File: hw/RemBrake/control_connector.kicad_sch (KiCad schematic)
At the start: 9 parts, among them J4 Conn_01x08_MountingPin, J5 Conn_01x04_MountingPin, J6 Conn_01x03_MountingPin

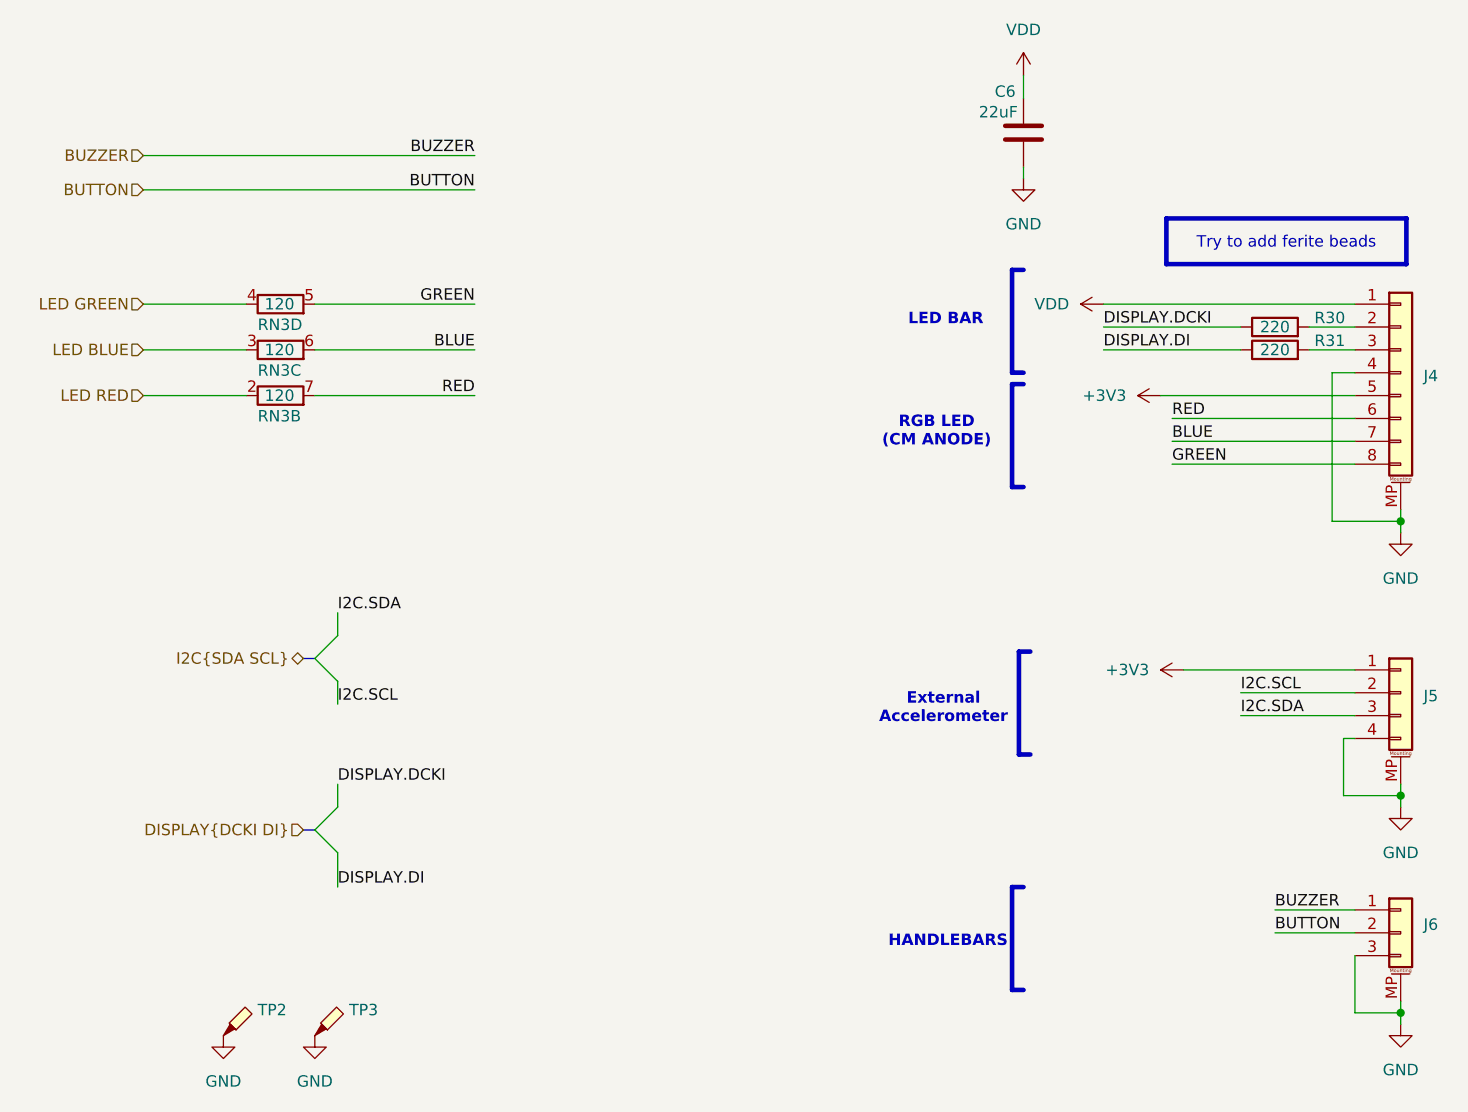
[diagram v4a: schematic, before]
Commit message: added resistor for the ideal diode enable and new annotation
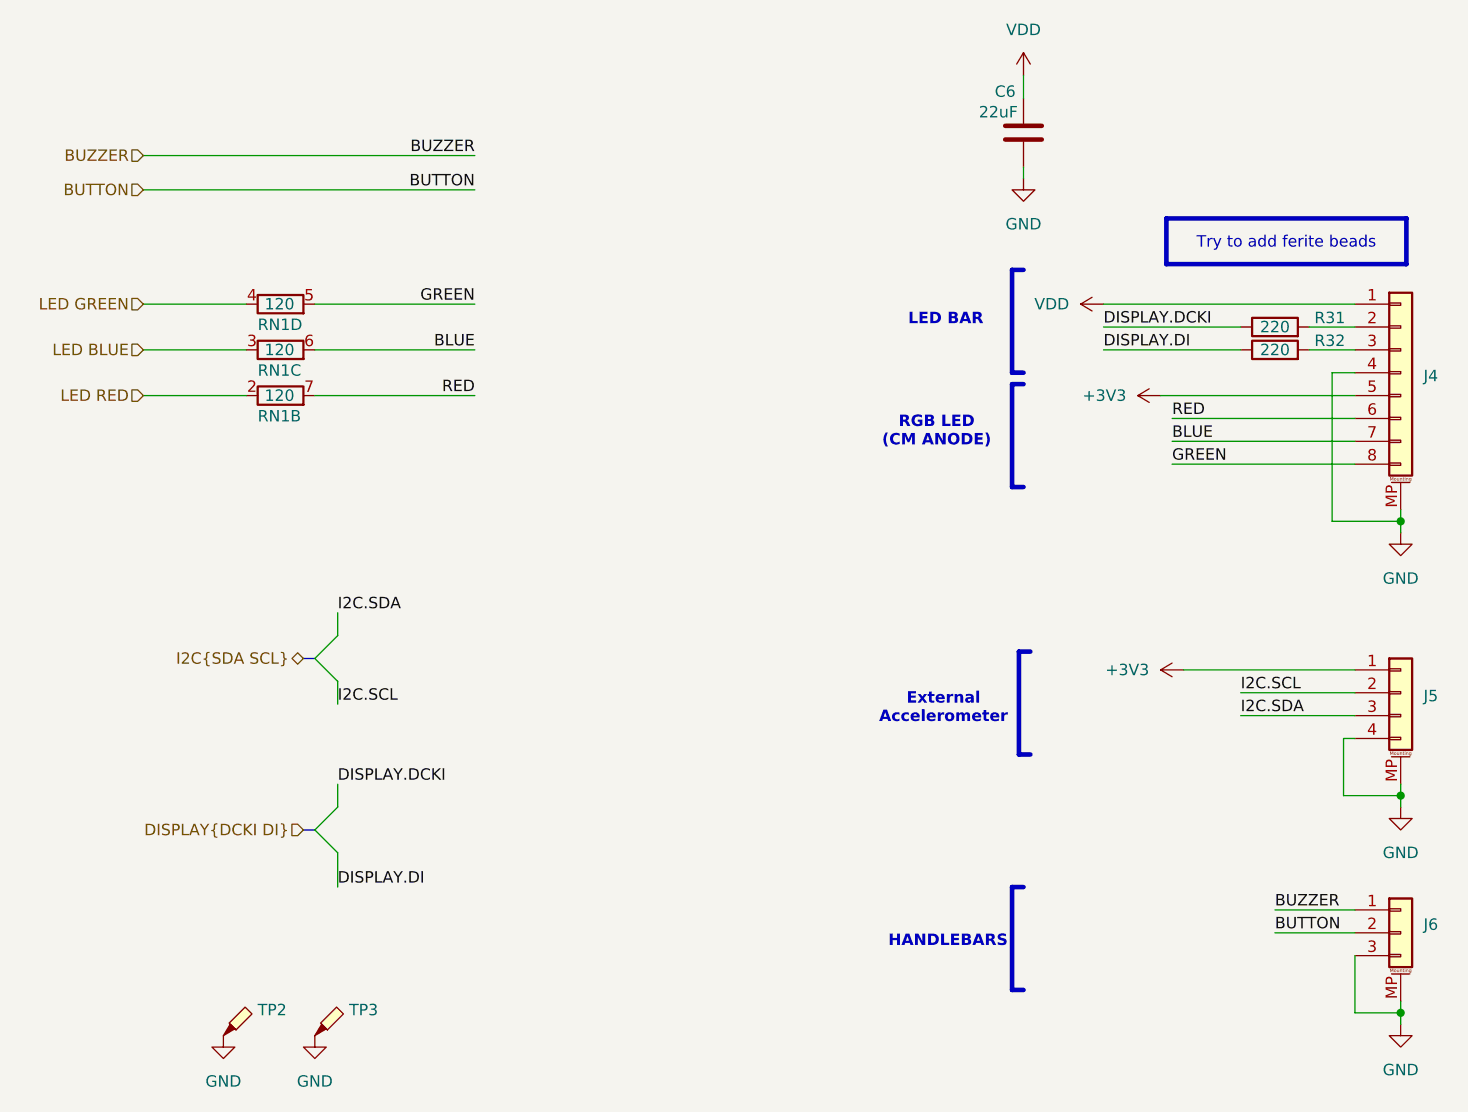
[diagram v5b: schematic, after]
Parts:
- renumbered R30 to R31, R31 to R32, RN3 to RN1
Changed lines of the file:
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@@
 		(dnp no)
 		(fields_autoplaced yes)
-		(property "Reference" "#PWR035"
+		(property "Reference" "#PWR034"
 			(at 96.52 146.05 0)
 			(hide yes)
@@
 			(project "RemBrake"
 				(path "/e6d4ae5b-c9d7-4cbe-b288-c929fdf55a75/c6fda42a-9645-46e5-b66a-57cf8664dccf"
-					(reference "#PWR035")
+					(reference "#PWR034")
 					(unit 1)
 				)
@@
 		(on_board yes)
 		(dnp no)
-		(property "Reference" "RN3"
+		(property "Reference" "RN1"
 			(at 90.17 70.866 90)
 			(effects
@@
 			(project "RemBrake"
 				(path "/e6d4ae5b-c9d7-4cbe-b288-c929fdf55a75/c6fda42a-9645-46e5-b66a-57cf8664dccf"
-					(reference "RN3")
+					(reference "RN1")
 					(unit 2)
 				)
@@
 		(dnp no)
 		(fields_autoplaced yes)
-		(property "Reference" "#PWR041"
+		(property "Reference" "#PWR039"
 			(at 196.85 99.06 0)
 			(hide yes)
@@
 			(project "RemBrake"
 				(path "/e6d4ae5b-c9d7-4cbe-b288-c929fdf55a75/c6fda42a-9645-46e5-b66a-57cf8664dccf"
-					(reference "#PWR041")
+					(reference "#PWR039")
 					(unit 1)
 				)
@@
 		(on_board yes)
 		(dnp no)
-		(property "Reference" "RN3"
+		(property "Reference" "RN1"
 			(at 90.17 60.706 90)
 			(effects
@@
 			(project ""
 				(path "/e6d4ae5b-c9d7-4cbe-b288-c929fdf55a75/c6fda42a-9645-46e5-b66a-57cf8664dccf"
-					(reference "RN3")
+					(reference "RN1")
 					(unit 4)
 				)
@@
 		(on_board yes)
 		(dnp no)
-		(property "Reference" "R30"
+		(property "Reference" "R31"
 			(at 209.296 59.944 90)
 			(effects
@@
 			(project "RemBrake"
 				(path "/e6d4ae5b-c9d7-4cbe-b288-c929fdf55a75/c6fda42a-9645-46e5-b66a-57cf8664dccf"
-					(reference "R30")
+					(reference "R31")
 					(unit 1)
 				)
@@
 		(dnp no)
 		(fields_autoplaced yes)
-		(property "Reference" "#PWR043"
+		(property "Reference" "#PWR041"
 			(at 217.17 120.65 0)
 			(hide yes)
@@
 			(project "RemBrake"
 				(path "/e6d4ae5b-c9d7-4cbe-b288-c929fdf55a75/c6fda42a-9645-46e5-b66a-57cf8664dccf"
-					(reference "#PWR043")
+					(reference "#PWR041")
 					(unit 1)
 				)
@@
 		(dnp no)
 		(fields_autoplaced yes)
-		(property "Reference" "#PWR037"
+		(property "Reference" "#PWR035"
 			(at 175.26 36.83 0)
 			(hide yes)
@@
 			(project "RemBrake"
 				(path "/e6d4ae5b-c9d7-4cbe-b288-c929fdf55a75/c6fda42a-9645-46e5-b66a-57cf8664dccf"
-					(reference "#PWR037")
+					(reference "#PWR035")
 					(unit 1)
 				)
@@
 		(dnp no)
 		(fields_autoplaced yes)
-		(property "Reference" "#PWR042"
+		(property "Reference" "#PWR040"
 			(at 217.17 90.17 0)
 			(hide yes)
@@
 			(project "RemBrake"
 				(path "/e6d4ae5b-c9d7-4cbe-b288-c929fdf55a75/c6fda42a-9645-46e5-b66a-57cf8664dccf"
-					(reference "#PWR042")
+					(reference "#PWR040")
 					(unit 1)
 				)
@@
 		(dnp no)
 		(fields_autoplaced yes)
-		(property "Reference" "#PWR038"
+		(property "Reference" "#PWR036"
 			(at 175.26 50.8 0)
 			(hide yes)
@@
 			(project "RemBrake"
 				(path "/e6d4ae5b-c9d7-4cbe-b288-c929fdf55a75/c6fda42a-9645-46e5-b66a-57cf8664dccf"
-					(reference "#PWR038")
+					(reference "#PWR036")
 					(unit 1)
 				)
@@
 		(dnp no)
 		(fields_autoplaced yes)
-		(property "Reference" "#PWR039"
+		(property "Reference" "#PWR037"
 			(at 187.96 58.42 0)
 			(hide yes)
@@
 			(project ""
 				(path "/e6d4ae5b-c9d7-4cbe-b288-c929fdf55a75/c6fda42a-9645-46e5-b66a-57cf8664dccf"
-					(reference "#PWR039")
+					(reference "#PWR037")
 					(unit 1)
 				)
@@
 		(on_board yes)
 		(dnp no)
-		(property "Reference" "R31"
+		(property "Reference" "R32"
 			(at 209.296 62.484 90)
 			(effects
@@
 			(project "RemBrake"
 				(path "/e6d4ae5b-c9d7-4cbe-b288-c929fdf55a75/c6fda42a-9645-46e5-b66a-57cf8664dccf"
-					(reference "R31")
+					(reference "R32")
 					(unit 1)
 				)
@@
 		(dnp no)
 		(fields_autoplaced yes)
-		(property "Reference" "#PWR034"
+		(property "Reference" "#PWR033"
 			(at 86.36 146.05 0)
 			(hide yes)
@@
 			(project "RemBrake"
 				(path "/e6d4ae5b-c9d7-4cbe-b288-c929fdf55a75/c6fda42a-9645-46e5-b66a-57cf8664dccf"
-					(reference "#PWR034")
+					(reference "#PWR033")
 					(unit 1)
 				)
@@
 		(dnp no)
 		(fields_autoplaced yes)
-		(property "Reference" "#PWR044"
+		(property "Reference" "#PWR042"
 			(at 217.17 144.78 0)
 			(hide yes)
@@
 			(project "RemBrake"
 				(path "/e6d4ae5b-c9d7-4cbe-b288-c929fdf55a75/c6fda42a-9645-46e5-b66a-57cf8664dccf"
-					(reference "#PWR044")
+					(reference "#PWR042")
 					(unit 1)
 				)
@@
 		(on_board yes)
 		(dnp no)
-		(property "Reference" "RN3"
+		(property "Reference" "RN1"
 			(at 90.17 65.786 90)
 			(effects
@@
 			(project "RemBrake"
 				(path "/e6d4ae5b-c9d7-4cbe-b288-c929fdf55a75/c6fda42a-9645-46e5-b66a-57cf8664dccf"
-					(reference "RN3")
+					(reference "RN1")
 					(unit 3)
 				)
@@
 		(dnp no)
 		(fields_autoplaced yes)
-		(property "Reference" "#PWR040"
+		(property "Reference" "#PWR038"
 			(at 194.31 68.58 0)
 			(hide yes)
@@
 			(project "RemBrake"
 				(path "/e6d4ae5b-c9d7-4cbe-b288-c929fdf55a75/c6fda42a-9645-46e5-b66a-57cf8664dccf"
-					(reference "#PWR040")
-					(unit 1)
-				)
+					(reference "#PWR038")
+					(unit 1)
+				)

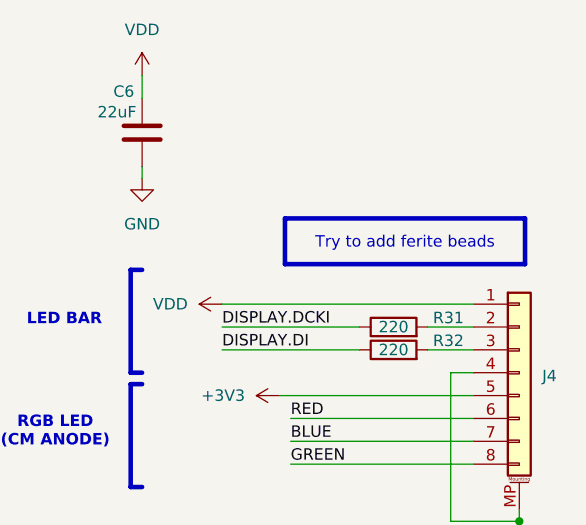
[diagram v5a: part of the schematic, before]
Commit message: finished new version of pcb with transistors gating vbus and fixed ledbar functionality
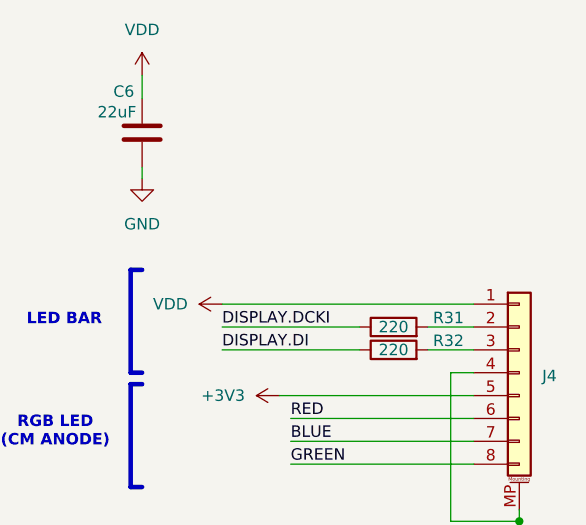
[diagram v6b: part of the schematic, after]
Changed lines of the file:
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@@
-		)
-	)
-	(text_box "Try to add ferite beads"
-		(exclude_from_sim no)
-		(at 191.135 48.895 0)
-		(size 26.67 5.08)
-		(margins 0.9525 0.9525 0.9525 0.9525)
-		(stroke
-			(width 0.508)
-			(type solid)
-			(color 128 63 0 1)
-		)
-		(fill
-			(type color)
-			(color 255 255 153 1)
-		)
-		(effects
-			(font
-				(size 1.27 1.27)
-			)
 		)
 	)

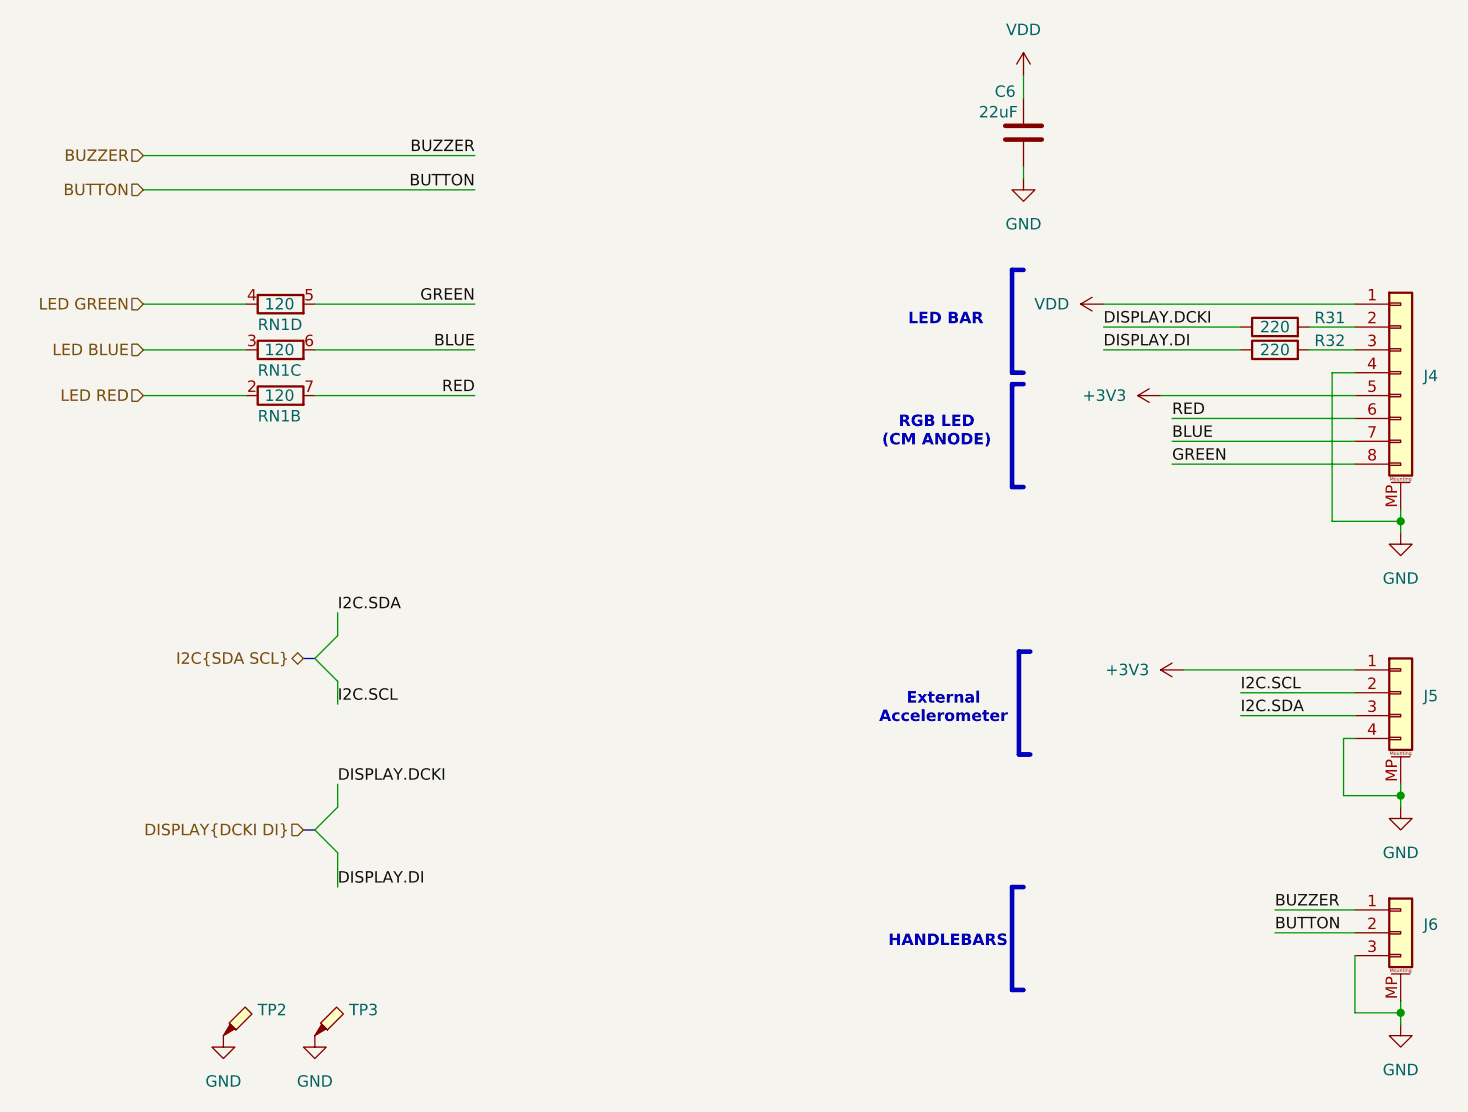
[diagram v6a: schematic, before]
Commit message: updated schematics and pcb - smd transistor was not connected to resistor to limit current through buzzer
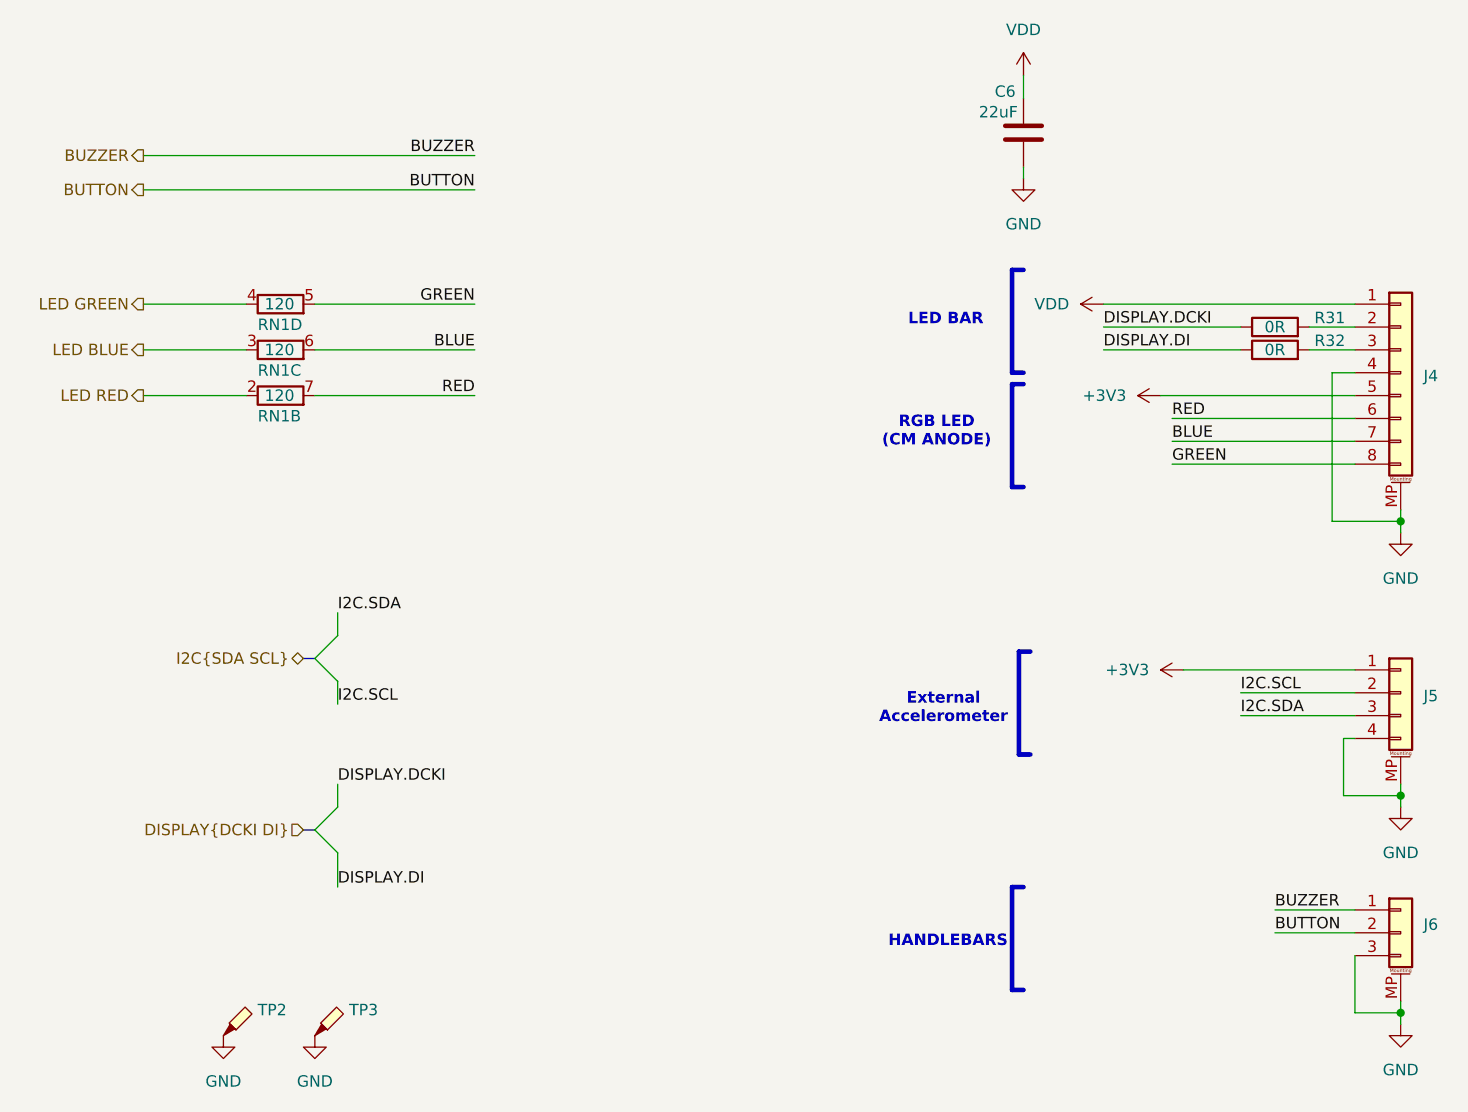
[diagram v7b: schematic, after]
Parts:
- R31, R32: value 220 -> 0R
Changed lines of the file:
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@@
 	)
 	(hierarchical_label "LED BLUE"
-		(shape input)
+		(shape output)
 		(at 77.47 63.5 180)
 		(effects
@@
 	)
 	(hierarchical_label "BUTTON"
-		(shape input)
+		(shape output)
 		(at 77.47 45.72 180)
 		(effects
@@
 	)
 	(hierarchical_label "BUZZER"
-		(shape input)
+		(shape output)
 		(at 77.47 41.91 180)
 		(effects
@@
 	)
 	(hierarchical_label "LED GREEN"
-		(shape input)
+		(shape output)
 		(at 77.47 58.42 180)
 		(effects
@@
 	)
 	(hierarchical_label "LED RED"
-		(shape input)
+		(shape output)
 		(at 77.47 68.58 180)
 		(effects
@@
 			)
 		)
-		(property "Value" "220"
+		(property "Value" "0R"
 			(at 203.2 60.96 90)
 			(effects
@@
 			)
 		)
-		(property "Value" "220"
+		(property "Value" "0R"
 			(at 203.2 63.5 90)
 			(effects
